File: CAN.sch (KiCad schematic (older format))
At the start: 6 parts, among them J2 Conn_01x02_Female, U2 MCP2562-H-SN

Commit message: reorganized schematic; added reverse polarity protection; start adding footprints
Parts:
- removed J2: Conn_01x02_Female, symbol Connector:Conn_01x02_Female
- added JP?: a, symbol Jumper:SolderJumper_2_Open
- C10: value C_Small -> 1uF
- C9: value C_Small -> 100nF
- R3: value R -> 120R
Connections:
- net labels added: CANH, CANL, RXD, TXD
- net labels removed: RX_CAN, TX_CAN
- wire segments 22 -> 24
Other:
- moved on the sheet: C10, C9, R3
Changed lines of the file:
@@
 $Descr A4 11693 8268
 encoding utf-8
-Sheet 2 7
+Sheet 2 9
 Title "PUTM_EV_Dashboard_2021"
 Date ""
@@
 U 1 1 61B06F42
 P 4450 3350
-F 0 "U2" H 4450 3928 50  0000 C CNN
-F 1 "MCP2562-H-SN" H 4450 3837 50  0000 C CNN
+F 0 "U2" H 4100 3700 50  0000 C CNN
+F 1 "MCP2562-H-SN" H 4800 3750 50  0000 C CNN
 F 2 "Package_SO:SOIC-8_3.9x4.9mm_P1.27mm" H 4450 2850 50  0001 C CIN
 F 3 "http://ww1.microchip.com/downloads/en/DeviceDoc/25167A.pdf" H 4450 3350 50  0001 C CNN
@@
 	1    4450 3750
 	1    0    0    -1
-$EndComp
-$Comp
-L power:GND #PWR0118
-U 1 1 61B070DF
-P 4250 2650
-F 0 "#PWR0118" H 4250 2400 50  0001 C CNN
-F 1 "GND" V 4255 2522 50  0000 R CNN
-F 2 "" H 4250 2650 50  0001 C CNN
-F 3 "" H 4250 2650 50  0001 C CNN
-	1    4250 2650
-	0    1    1    0
 $EndComp
 $Comp
@@
 L power:GND #PWR0121
 U 1 1 61B07269
-P 3500 3650
-F 0 "#PWR0121" H 3500 3400 50  0001 C CNN
-F 1 "GND" H 3505 3477 50  0000 C CNN
-F 2 "" H 3500 3650 50  0001 C CNN
-F 3 "" H 3500 3650 50  0001 C CNN
-	1    3500 3650
+P 3400 3750
+F 0 "#PWR0121" H 3400 3500 50  0001 C CNN
+F 1 "GND" H 3405 3577 50  0000 C CNN
+F 2 "" H 3400 3750 50  0001 C CNN
+F 3 "" H 3400 3750 50  0001 C CNN
+	1    3400 3750
 	1    0    0    -1
 $EndComp
@@
 L Device:C_Small C9
 U 1 1 61B072AA
-P 3500 3550
-F 0 "C9" H 3592 3596 50  0000 L CNN
-F 1 "C_Small" H 3592 3505 50  0000 L CNN
-F 2 "" H 3500 3550 50  0001 C CNN
-F 3 "~" H 3500 3550 50  0001 C CNN
-	1    3500 3550
-	1    0    0    -1
-$EndComp
-Wire Wire Line
-	3250 3450 3500 3450
-Wire Wire Line
-	3500 3450 3950 3450
-Connection ~ 3500 3450
-$Comp
-L Device:C_Small C10
-U 1 1 61B0746F
-P 4350 2650
-F 0 "C10" V 4121 2650 50  0000 C CNN
-F 1 "C_Small" V 4212 2650 50  0000 C CNN
-F 2 "" H 4350 2650 50  0001 C CNN
-F 3 "~" H 4350 2650 50  0001 C CNN
-	1    4350 2650
-	0    1    1    0
-$EndComp
-Wire Wire Line
-	4450 2450 4450 2650
-Connection ~ 4450 2650
-Wire Wire Line
-	4450 2650 4450 2950
-Wire Wire Line
-	3700 3150 3950 3150
-Wire Wire Line
-	3700 3250 3950 3250
-Text GLabel 3700 3150 0    50   Input ~ 0
-TX_CAN
-Text GLabel 3700 3250 0    50   Input ~ 0
-RX_CAN
+P 3400 3650
+F 0 "C9" H 3492 3696 50  0000 L CNN
+F 1 "100nF" H 3492 3605 50  0000 L CNN
+F 2 "" H 3400 3650 50  0001 C CNN
+F 3 "~" H 3400 3650 50  0001 C CNN
+	1    3400 3650
+	1    0    0    -1
+$EndComp
 $Comp
 L Device:R R3
 U 1 1 61B077A7
-P 5250 3350
-F 0 "R3" H 5320 3396 50  0000 L CNN
-F 1 "R" H 5320 3305 50  0000 L CNN
-F 2 "" V 5180 3350 50  0001 C CNN
-F 3 "~" H 5250 3350 50  0001 C CNN
-	1    5250 3350
+P 6700 3500
+F 0 "R3" H 6770 3546 50  0000 L CNN
+F 1 "120R" H 6770 3455 50  0000 L CNN
+F 2 "" V 6630 3500 50  0001 C CNN
+F 3 "~" H 6700 3500 50  0001 C CNN
+	1    6700 3500
 	1    0    0    -1
 $EndComp
@@
 	4950 3250 5050 3250
 Wire Wire Line
-	5050 3250 5050 3200
-Wire Wire Line
-	5050 3200 5250 3200
-Wire Wire Line
 	4950 3450 5050 3450
-Wire Wire Line
-	5050 3450 5050 3500
-Wire Wire Line
-	5050 3500 5250 3500
 $Comp
 L Device:D_TVS_x2_AAC D1
@@
 $EndComp
 Wire Wire Line
-	5050 3200 5050 3000
-Wire Wire Line
 	5050 3000 6000 3000
-Connection ~ 5050 3200
-Wire Wire Line
-	5050 3500 5050 3700
 Wire Wire Line
 	5050 3700 6000 3700
-Connection ~ 5050 3500
 Connection ~ 6000 3700
-$Comp
-L Connector:Conn_01x02_Female J2
-U 1 1 61B0811E
-P 7050 3300
-F 0 "J2" H 7077 3276 50  0000 L CNN
-F 1 "Conn_01x02_Female" H 7077 3185 50  0000 L CNN
-F 2 "" H 7050 3300 50  0001 C CNN
-F 3 "~" H 7050 3300 50  0001 C CNN
-	1    7050 3300
-	1    0    0    -1
-$EndComp
-Wire Wire Line
-	6850 3700 6850 3400
-Wire Wire Line
-	6000 3700 6850 3700
-Wire Wire Line
-	6850 3300 6850 3000
-Wire Wire Line
-	6850 3000 6000 3000
 Connection ~ 6000 3000
+Text HLabel 2900 3150 0    50   Input ~ 0
+TXD
+Text HLabel 2900 3250 0    50   Output ~ 0
+RXD
+Wire Wire Line
+	2900 3150 3950 3150
+Wire Wire Line
+	2900 3250 3950 3250
+Wire Wire Line
+	3250 3450 3400 3450
+Wire Wire Line
+	3400 3550 3400 3450
+Connection ~ 3400 3450
+Wire Wire Line
+	3400 3450 3950 3450
+Wire Wire Line
+	5050 3000 5050 3250
+Wire Wire Line
+	5050 3450 5050 3700
+Text HLabel 7250 3000 2    50   BiDi ~ 0
+CANH
+Text HLabel 7250 3700 2    50   BiDi ~ 0
+CANL
+Wire Wire Line
+	6000 3000 6700 3000
+Wire Wire Line
+	6000 3700 6700 3700
+$Comp
+L Jumper:SolderJumper_2_Open JP?
+U 1 1 5FD7AB56
+P 6700 3200
+F 0 "JP?" V 6700 3268 50  0000 L CNN
+F 1 "a" V 6745 3268 50  0001 L CNN
+F 2 "" H 6700 3200 50  0001 C CNN
+F 3 "~" H 6700 3200 50  0001 C CNN
+	1    6700 3200
+	0    1    1    0
+$EndComp
+Wire Wire Line
+	6700 3050 6700 3000
+Connection ~ 6700 3000
+Wire Wire Line
+	6700 3000 7250 3000
+Wire Wire Line
+	6700 3650 6700 3700
+Connection ~ 6700 3700
+Wire Wire Line
+	6700 3700 7250 3700
+$Comp
+L Device:C_Small C10
+U 1 1 61B0746F
+P 3800 2650
+F 0 "C10" V 3571 2650 50  0000 C CNN
+F 1 "1uF" V 3662 2650 50  0000 C CNN
+F 2 "" H 3800 2650 50  0001 C CNN
+F 3 "~" H 3800 2650 50  0001 C CNN
+	1    3800 2650
+	1    0    0    -1
+$EndComp
+Wire Wire Line
+	3800 2800 3800 2750
+Wire Wire Line
+	4450 2450 4450 2500
+Wire Wire Line
+	3800 2550 3800 2500
+Wire Wire Line
+	3800 2500 4450 2500
+Connection ~ 4450 2500
+Wire Wire Line
+	4450 2500 4450 2950
+$Comp
+L power:GND #PWR?
+U 1 1 5FD7F8A4
+P 3800 2800
+F 0 "#PWR?" H 3800 2550 50  0001 C CNN
+F 1 "GND" H 3805 2627 50  0000 C CNN
+F 2 "" H 3800 2800 50  0001 C CNN
+F 3 "" H 3800 2800 50  0001 C CNN
+	1    3800 2800
+	1    0    0    -1
+$EndComp
 $EndSCHEMATC

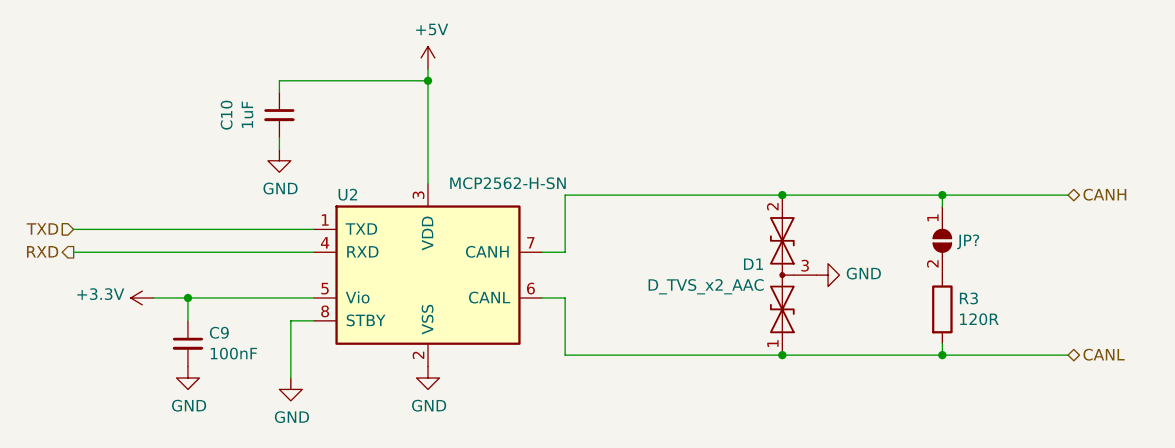
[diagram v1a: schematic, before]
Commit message: footprints; library for 7seg; start pcb layout
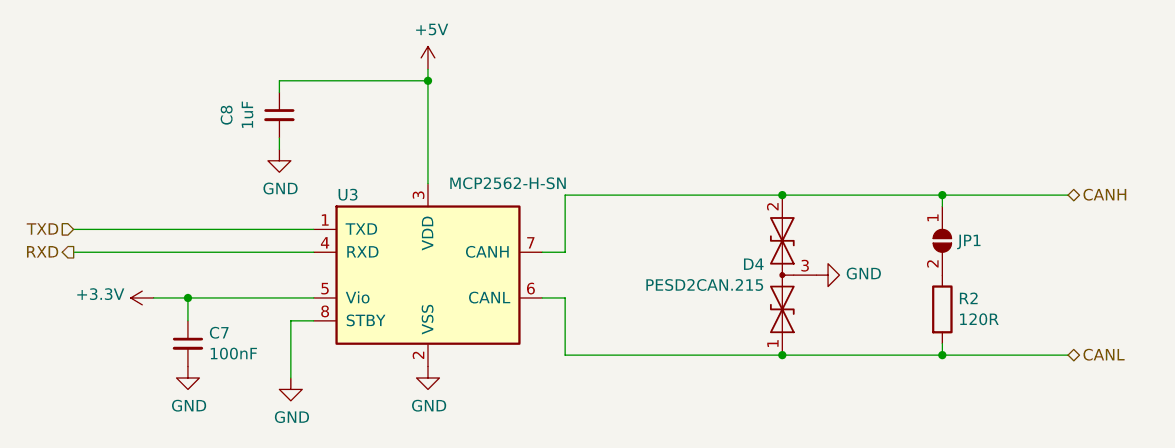
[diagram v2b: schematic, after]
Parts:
- C7: renamed from C9; footprint (none) -> Capacitor_SMD:C_0603_1608Metric
- C8: renamed from C10; footprint (none) -> Capacitor_SMD:C_0603_1608Metric
- D4: renamed from D1; value D_TVS_x2_AAC -> PESD2CAN.215; footprint (none) -> Package_TO_SOT_SMD:SOT-23
- JP1: renamed from JP?; footprint (none) -> Jumper:SolderJumper-2_P1.3mm_Open_TrianglePad1.0x1.5mm
- R2: renamed from R3; footprint (none) -> Resistor_SMD:R_0603_1608Metric
- renumbered U2 to U3
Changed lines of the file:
@@
 $EndDescr
 $Comp
-L Interface_CAN_LIN:MCP2562-H-SN U2
+L Interface_CAN_LIN:MCP2562-H-SN U3
 U 1 1 61B06F42
 P 4450 3350
-F 0 "U2" H 4100 3700 50  0000 C CNN
+F 0 "U3" H 4100 3700 50  0000 C CNN
 F 1 "MCP2562-H-SN" H 4800 3750 50  0000 C CNN
 F 2 "Package_SO:SOIC-8_3.9x4.9mm_P1.27mm" H 4450 2850 50  0001 C CIN
@@
 $EndComp
 $Comp
-L power:GND #PWR0116
+L power:GND #PWR09
 U 1 1 61B06FE5
 P 3850 3800
-F 0 "#PWR0116" H 3850 3550 50  0001 C CNN
+F 0 "#PWR09" H 3850 3550 50  0001 C CNN
 F 1 "GND" H 3855 3627 50  0000 C CNN
 F 2 "" H 3850 3800 50  0001 C CNN
@@
 	3850 3550 3850 3800
 $Comp
-L power:GND #PWR0117
+L power:GND #PWR011
 U 1 1 61B0700C
 P 4450 3750
-F 0 "#PWR0117" H 4450 3500 50  0001 C CNN
+F 0 "#PWR011" H 4450 3500 50  0001 C CNN
 F 1 "GND" H 4455 3577 50  0000 C CNN
 F 2 "" H 4450 3750 50  0001 C CNN
@@
 $EndComp
 $Comp
-L power:+5V #PWR0119
+L power:+5V #PWR010
 U 1 1 61B0717A
 P 4450 2450
-F 0 "#PWR0119" H 4450 2300 50  0001 C CNN
+F 0 "#PWR010" H 4450 2300 50  0001 C CNN
 F 1 "+5V" H 4465 2623 50  0000 C CNN
 F 2 "" H 4450 2450 50  0001 C CNN
@@
 $EndComp
 $Comp
-L power:+3.3V #PWR0120
+L power:+3.3V #PWR06
 U 1 1 61B07202
 P 3250 3450
-F 0 "#PWR0120" H 3250 3300 50  0001 C CNN
+F 0 "#PWR06" H 3250 3300 50  0001 C CNN
 F 1 "+3.3V" V 3265 3578 50  0000 L CNN
 F 2 "" H 3250 3450 50  0001 C CNN
@@
 $EndComp
 $Comp
-L power:GND #PWR0121
+L power:GND #PWR07
 U 1 1 61B07269
 P 3400 3750
-F 0 "#PWR0121" H 3400 3500 50  0001 C CNN
+F 0 "#PWR07" H 3400 3500 50  0001 C CNN
 F 1 "GND" H 3405 3577 50  0000 C CNN
 F 2 "" H 3400 3750 50  0001 C CNN
@@
 $EndComp
 $Comp
-L Device:C_Small C9
+L Device:C_Small C7
 U 1 1 61B072AA
 P 3400 3650
-F 0 "C9" H 3492 3696 50  0000 L CNN
+F 0 "C7" H 3492 3696 50  0000 L CNN
 F 1 "100nF" H 3492 3605 50  0000 L CNN
-F 2 "" H 3400 3650 50  0001 C CNN
+F 2 "Capacitor_SMD:C_0603_1608Metric" H 3400 3650 50  0001 C CNN
 F 3 "~" H 3400 3650 50  0001 C CNN
 	1    3400 3650
@@
 $EndComp
 $Comp
-L Device:R R3
+L Device:R R2
 U 1 1 61B077A7
 P 6700 3500
-F 0 "R3" H 6770 3546 50  0000 L CNN
+F 0 "R2" H 6770 3546 50  0000 L CNN
 F 1 "120R" H 6770 3455 50  0000 L CNN
-F 2 "" V 6630 3500 50  0001 C CNN
+F 2 "Resistor_SMD:R_0603_1608Metric" V 6630 3500 50  0001 C CNN
 F 3 "~" H 6700 3500 50  0001 C CNN
 	1    6700 3500
@@
 	4950 3450 5050 3450
 $Comp
-L Device:D_TVS_x2_AAC D1
+L Device:D_TVS_x2_AAC D4
 U 1 1 61B07D4F
 P 6000 3350
-F 0 "D1" V 6046 3428 50  0000 L CNN
-F 1 "D_TVS_x2_AAC" V 5955 3428 50  0000 L CNN
-F 2 "" H 5850 3350 50  0001 C CNN
+F 0 "D4" V 6046 3428 50  0000 L CNN
+F 1 "PESD2CAN.215" V 5955 3428 50  0000 L CNN
+F 2 "Package_TO_SOT_SMD:SOT-23" H 5850 3350 50  0001 C CNN
 F 3 "~" H 5850 3350 50  0001 C CNN
 	1    6000 3350
@@
 $EndComp
 $Comp
-L power:GND #PWR0122
+L power:GND #PWR012
 U 1 1 61B07DCB
 P 6150 3350
-F 0 "#PWR0122" H 6150 3100 50  0001 C CNN
+F 0 "#PWR012" H 6150 3100 50  0001 C CNN
 F 1 "GND" V 6155 3222 50  0000 R CNN
 F 2 "" H 6150 3350 50  0001 C CNN
@@
 	6000 3700 6700 3700
 $Comp
-L Jumper:SolderJumper_2_Open JP?
+L Jumper:SolderJumper_2_Open JP1
 U 1 1 5FD7AB56
 P 6700 3200
-F 0 "JP?" V 6700 3268 50  0000 L CNN
+F 0 "JP1" V 6700 3268 50  0000 L CNN
 F 1 "a" V 6745 3268 50  0001 L CNN
-F 2 "" H 6700 3200 50  0001 C CNN
+F 2 "Jumper:SolderJumper-2_P1.3mm_Open_TrianglePad1.0x1.5mm" H 6700 3200 50  0001 C CNN
 F 3 "~" H 6700 3200 50  0001 C CNN
 	1    6700 3200
@@
 	6700 3700 7250 3700
 $Comp
-L Device:C_Small C10
+L Device:C_Small C8
 U 1 1 61B0746F
 P 3800 2650
-F 0 "C10" V 3571 2650 50  0000 C CNN
+F 0 "C8" V 3571 2650 50  0000 C CNN
 F 1 "1uF" V 3662 2650 50  0000 C CNN
-F 2 "" H 3800 2650 50  0001 C CNN
+F 2 "Capacitor_SMD:C_0603_1608Metric" H 3800 2650 50  0001 C CNN
 F 3 "~" H 3800 2650 50  0001 C CNN
 	1    3800 2650
@@
 	4450 2500 4450 2950
 $Comp
-L power:GND #PWR?
+L power:GND #PWR08
 U 1 1 5FD7F8A4
 P 3800 2800
-F 0 "#PWR?" H 3800 2550 50  0001 C CNN
+F 0 "#PWR08" H 3800 2550 50  0001 C CNN
 F 1 "GND" H 3805 2627 50  0000 C CNN
 F 2 "" H 3800 2800 50  0001 C CNN
